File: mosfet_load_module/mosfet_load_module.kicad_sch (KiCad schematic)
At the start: 46 parts, among them J1 Conn_01x03_Pin, J2 Conn_01x03_Pin, J3 Conn_01x03_Pin, J4 Conn_01x05_Pin, J5 Conn_01x05_Pin, J6 Conn_01x03_Pin, J7 Conn_01x03_Pin, Q1 IPP060N06N, Q2 BC817, Q3 BC817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

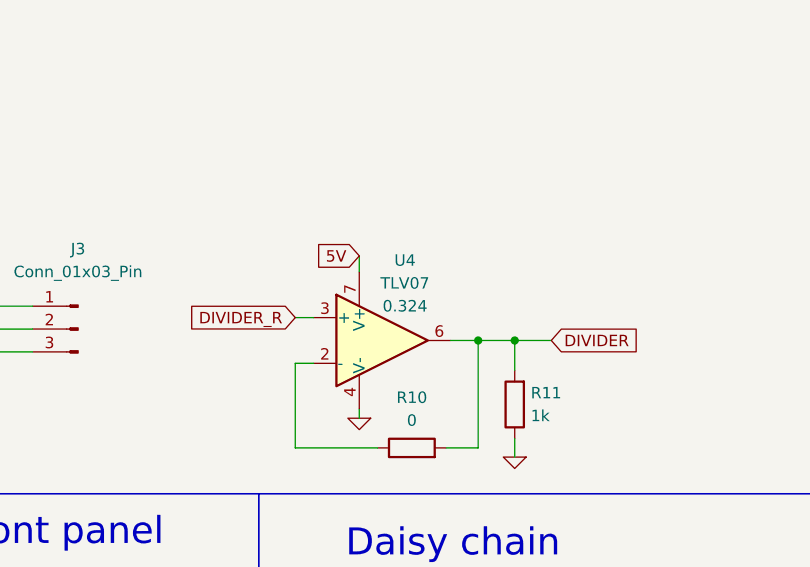
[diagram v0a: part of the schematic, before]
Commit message: Konačno PCB za BJT modul je počeo.
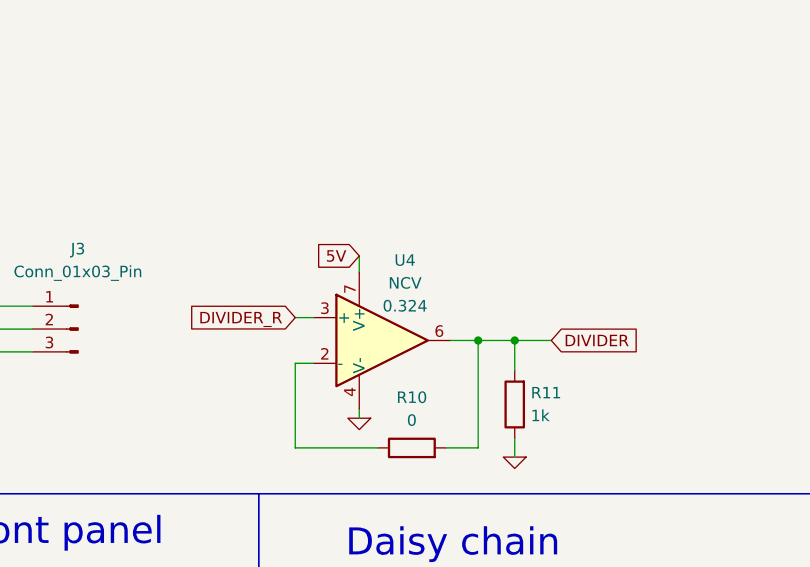
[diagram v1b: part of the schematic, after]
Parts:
- U4: value TLV07 -> NCV
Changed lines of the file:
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@@
       (effects (font (size 1.27 1.27)))
     )
-    (property "Value" "TLV07" (at 95.504 59.69 0)
+    (property "Value" "NCV" (at 95.504 59.69 0)
       (effects (font (size 1.27 1.27)))
     )
